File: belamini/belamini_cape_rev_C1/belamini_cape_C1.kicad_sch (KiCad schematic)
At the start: 0 parts

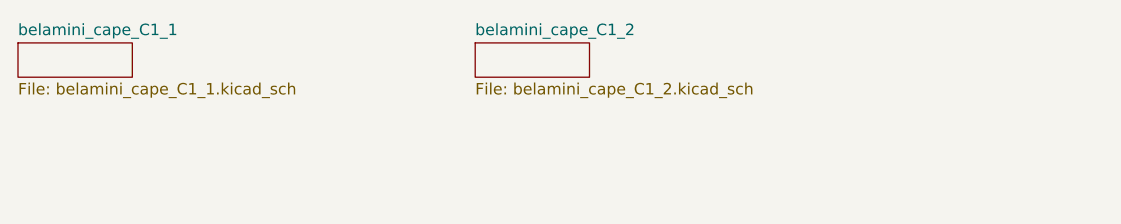
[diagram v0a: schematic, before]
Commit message: Add logo to Mini rev. C1, clean up schematic and add production files
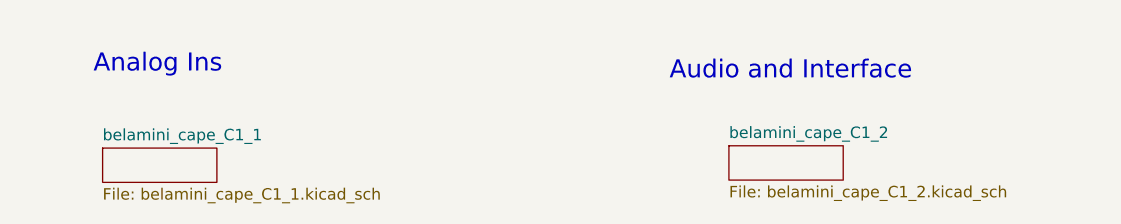
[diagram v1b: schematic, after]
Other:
- note added: "Analog Ins"
- note added: "Audio and Interface"
- company: (none) -> Augmented Instruments Ltd
- title: (none) -> Bela Mini
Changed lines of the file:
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@@
 (kicad_sch (version 20211123) (generator eeschema)
   (paper "A4")
-  (sheet (at 25.4 25.4) (size 12.7 3.81) (fields_autoplaced)
+  (title_block
+    (title "Bela Mini")
+    (date "2022-03-26")
+    (rev "C1")
+    (company "Augmented Instruments Ltd")
+  )
+  (text "Analog Ins" (at 33.782 28.956 0)
+    (effects (font (size 2 2)) (justify left bottom))
+  )
+  (text "Audio and Interface" (at 97.79 29.718 0)
+    (effects (font (size 2 2)) (justify left bottom))
+  )
+  (sheet (at 34.798 37.084) (size 12.7 3.81) (fields_autoplaced)
     (stroke (width 0) (type solid) (color 0 0 0 0))
     (fill (color 0 0 0 0.0000))
-    (property "Sheet name" "belamini_cape_C1_1" (id 0) (at 25.4 24.6884 0)
+    (property "Sheet name" "belamini_cape_C1_1" (id 0) (at 34.798 36.3724 0)
       (effects (font (size 1.27 1.27)) (justify left bottom))
     )
-    (property "Sheet file" "belamini_cape_C1_1.kicad_sch" (id 1) (at 25.4 29.7946 0)
+    (property "Sheet file" "belamini_cape_C1_1.kicad_sch" (id 1) (at 34.798 41.4786 0)
       (effects (font (size 1.27 1.27)) (justify left top))
     )
   )
-  (sheet (at 76.2 25.4) (size 12.7 3.81) (fields_autoplaced)
+  (sheet (at 104.394 36.83) (size 12.7 3.81) (fields_autoplaced)
     (stroke (width 0) (type solid) (color 0 0 0 0))
     (fill (color 0 0 0 0.0000))
-    (property "Sheet name" "belamini_cape_C1_2" (id 0) (at 76.2 24.6884 0)
+    (property "Sheet name" "belamini_cape_C1_2" (id 0) (at 104.394 36.1184 0)
       (effects (font (size 1.27 1.27)) (justify left bottom))
     )
-    (property "Sheet file" "belamini_cape_C1_2.kicad_sch" (id 1) (at 76.2 29.7946 0)
+    (property "Sheet file" "belamini_cape_C1_2.kicad_sch" (id 1) (at 104.394 41.2246 0)
       (effects (font (size 1.27 1.27)) (justify left top))
     )
@@
     )
     (path "/c15b31bd-285d-498f-b04e-55d8a4c43e67/6b6aa791-0e9c-4dd1-89d9-fd83d4045be1"
-      (reference "D1") (unit 1) (value "ESD") (footprint "Diode_SMD:D_0603_1608Metric")
+      (reference "D1") (unit 1) (value "PESD0603-240") (footprint "Diode_SMD:D_0603_1608Metric")
     )
     (path "/c15b31bd-285d-498f-b04e-55d8a4c43e67/869a6a78-2df7-4e21-8ab9-bd4868a7773f"
-      (reference "D2") (unit 1) (value "ESD") (footprint "Diode_SMD:D_0603_1608Metric")
+      (reference "D2") (unit 1) (value "PESD0603-240") (footprint "Diode_SMD:D_0603_1608Metric")
     )
     (path "/c15b31bd-285d-498f-b04e-55d8a4c43e67/cbccfdca-fb5f-461e-ae52-a6c13d8e2642"
@@
     )
     (path "/c15b31bd-285d-498f-b04e-55d8a4c43e67/d65f6660-8da2-41ad-8c60-a36b33b51cc0"
-      (reference "D5") (unit 1) (value "LED_Dual_AAKK") (footprint "LED_SMD:LED_LiteOn_LTST-C19HE1WT")
+      (reference "D5") (unit 1) (value "LTST-C195TBJRKT") (footprint "LED_SMD:LED_LiteOn_LTST-C19HE1WT")
     )
     (path "/97f314f7-06f7-4f76-bef3-e5a7c3bbe098/6e0fe158-ffc5-4a8f-94d6-3545c71bab7e"
-      (reference "FB1") (unit 1) (value "FerriteBead") (footprint "Inductor_SMD:L_0603_1608Metric")
+      (reference "FB1") (unit 1) (value "MPZ1608S121ATAH0") (footprint "Inductor_SMD:L_0603_1608Metric")
     )
     (path "/c15b31bd-285d-498f-b04e-55d8a4c43e67/4e92241f-8d90-4676-97dd-3daf3c557d71"
-      (reference "FB2") (unit 1) (value "FerriteBead") (footprint "Inductor_SMD:L_0603_1608Metric")
+      (reference "FB2") (unit 1) (value "MPZ1608S121ATAH0") (footprint "Inductor_SMD:L_0603_1608Metric")
     )
     (path "/97f314f7-06f7-4f76-bef3-e5a7c3bbe098/9dacd6eb-de6a-4d25-b9a4-7594fa54cc34"
@@
     )
     (path "/c15b31bd-285d-498f-b04e-55d8a4c43e67/5705ea15-5e4c-4d32-bdb8-8bc266d84b62"
-      (reference "S1") (unit 1) (value "SW_Push") (footprint "Button_Switch_SMD:SW_SPST_PTS810")
-    )
-  )
+      (reference "S1") (unit 1) (value "PTS810") (footprint "Button_Switch_SMD:SW_SPST_PTS810")
+    )
+  )
